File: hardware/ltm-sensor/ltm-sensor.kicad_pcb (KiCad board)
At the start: 2 copper layers, 89.7 x 53 mm, 22 parts, among them J1 KE PCB UTAMA, Q1 AO3400, U1 ITR20001 (S1), U2 ITR20001 (S2), U3 ITR20001 (S3), U4 ITR20001 (S4), U5 ITR20001 (S5)

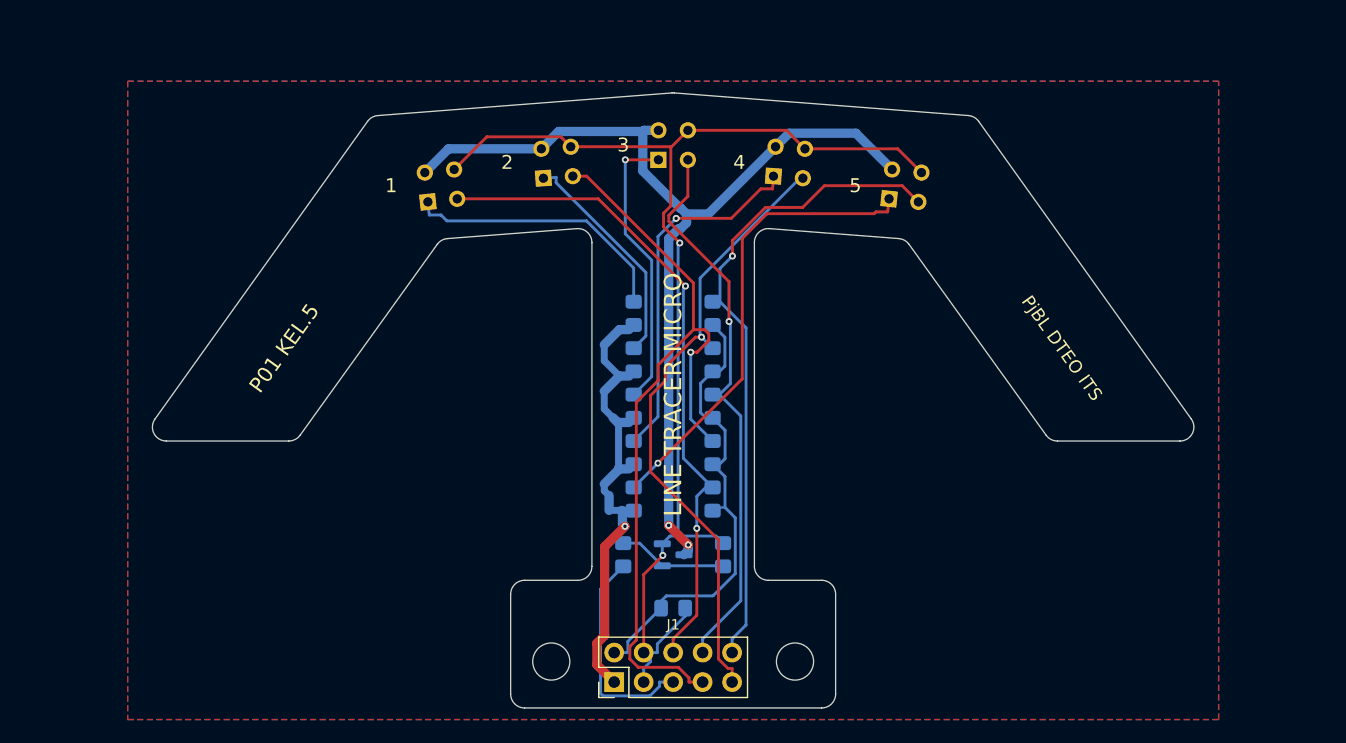
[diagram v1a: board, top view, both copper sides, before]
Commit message: Sensor 16 titik + mux + LED, kabel pita, aturan cetak 0,8 mm
- PCB sensor v2: batang lurus 110 x 51 mm, 16x ITR20001 (jarak 6,5 mm),
  modul mux CD74HC4067, MCP23017 + 16 LED indikator, box header IDC J1
- PCB utama: J5 jadi box header IDC 2x6 (kabel pita ke PCB sensor),
  pin ESP32 disusun ulang supaya jalur tidak saling silang
- Aturan tempat cetak: jalur >= 0,8 mm (daya 1,2), clearance 0,5,
  via 1,6/0,8; kedua PCB 0 jalur putus, DRC bersih
- Charter/RAB: 16 sensor, total Rp896.000
- Model 3D v12: PCB sensor batang di dudukan 3D print + kabel pita,
  STEP dan render diperbarui

Co-Authored-By: Claude Opus 5.5 <noreply@anthropic.com>
Claude-Session: https://claude.ai/code/session_016j7fGnGXJh3ke3RU3C9DKW
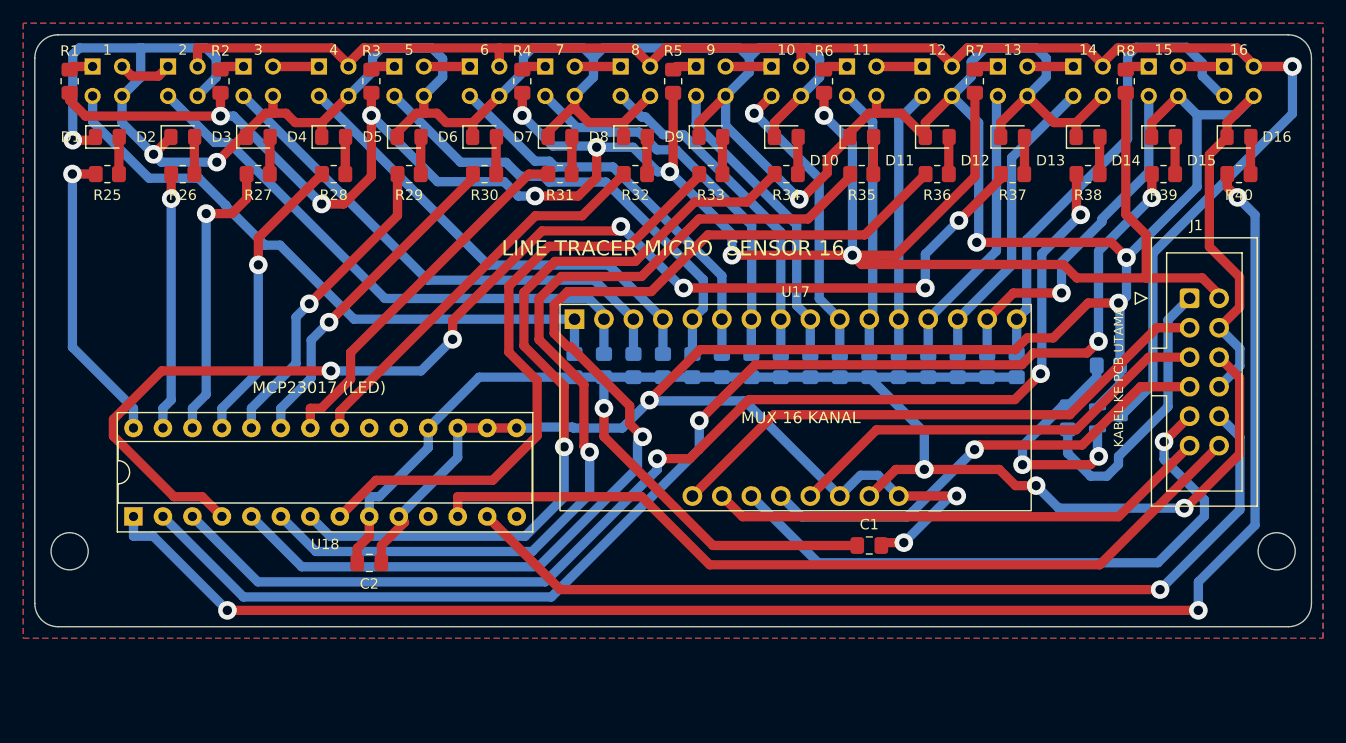
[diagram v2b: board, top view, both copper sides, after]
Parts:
- added C2: 100nF, Capacitor_SMD:C_0805_2012Metric_Pad1.18x1.45mm_HandSolder, F.Cu at (73.8, 58.5)
- added D1: LED, LED_SMD:LED_0805_2012Metric_Pad1.15x1.40mm_HandSolder, F.Cu at (51.2, 21.8)
- added D10: LED, LED_SMD:LED_0805_2012Metric_Pad1.15x1.40mm_HandSolder, F.Cu at (109.8, 21.8)
- added D11: LED, LED_SMD:LED_0805_2012Metric_Pad1.15x1.40mm_HandSolder, F.Cu at (116.2, 21.8)
- added D12: LED, LED_SMD:LED_0805_2012Metric_Pad1.15x1.40mm_HandSolder, F.Cu at (122.8, 21.8)
- added D13: LED, LED_SMD:LED_0805_2012Metric_Pad1.15x1.40mm_HandSolder, F.Cu at (129.2, 21.8)
- added D14: LED, LED_SMD:LED_0805_2012Metric_Pad1.15x1.40mm_HandSolder, F.Cu at (135.8, 21.8)
- added D15: LED, LED_SMD:LED_0805_2012Metric_Pad1.15x1.40mm_HandSolder, F.Cu at (142.2, 21.8)
- added D16: LED, LED_SMD:LED_0805_2012Metric_Pad1.15x1.40mm_HandSolder, F.Cu at (148.8, 21.8)
- added D2: LED, LED_SMD:LED_0805_2012Metric_Pad1.15x1.40mm_HandSolder, F.Cu at (57.8, 21.8)
- added D3: LED, LED_SMD:LED_0805_2012Metric_Pad1.15x1.40mm_HandSolder, F.Cu at (64.2, 21.8)
- added D4: LED, LED_SMD:LED_0805_2012Metric_Pad1.15x1.40mm_HandSolder, F.Cu at (70.8, 21.8)
- added D5: LED, LED_SMD:LED_0805_2012Metric_Pad1.15x1.40mm_HandSolder, F.Cu at (77.2, 21.8)
- added D6: LED, LED_SMD:LED_0805_2012Metric_Pad1.15x1.40mm_HandSolder, F.Cu at (83.8, 21.8)
- added D7: LED, LED_SMD:LED_0805_2012Metric_Pad1.15x1.40mm_HandSolder, F.Cu at (90.2, 21.8)
- added D8: LED, LED_SMD:LED_0805_2012Metric_Pad1.15x1.40mm_HandSolder, F.Cu at (96.8, 21.8)
- added D9: LED, LED_SMD:LED_0805_2012Metric_Pad1.15x1.40mm_HandSolder, F.Cu at (103.2, 21.8)
- added R13: 10k, Resistor_SMD:R_0805_2012Metric_Pad1.20x1.40mm_HandSolder, B.Cu at (101.7, 41.5)
- added R14: 10k, Resistor_SMD:R_0805_2012Metric_Pad1.20x1.40mm_HandSolder, B.Cu at (104.2, 41.5)
- added R15: 10k, Resistor_SMD:R_0805_2012Metric_Pad1.20x1.40mm_HandSolder, B.Cu at (106.7, 41.5)
- added R16: 10k, Resistor_SMD:R_0805_2012Metric_Pad1.20x1.40mm_HandSolder, B.Cu at (109.3, 41.5)
- added R17: 10k, Resistor_SMD:R_0805_2012Metric_Pad1.20x1.40mm_HandSolder, B.Cu at (111.8, 41.5)
- added R18: 10k, Resistor_SMD:R_0805_2012Metric_Pad1.20x1.40mm_HandSolder, B.Cu at (114.4, 41.5)
- added R19: 10k, Resistor_SMD:R_0805_2012Metric_Pad1.20x1.40mm_HandSolder, B.Cu at (116.9, 41.5)
- added R20: 10k, Resistor_SMD:R_0805_2012Metric_Pad1.20x1.40mm_HandSolder, B.Cu at (119.4, 41.5)
- added R21: 10k, Resistor_SMD:R_0805_2012Metric_Pad1.20x1.40mm_HandSolder, B.Cu at (122.0, 41.5)
- added R22: 10k, Resistor_SMD:R_0805_2012Metric_Pad1.20x1.40mm_HandSolder, B.Cu at (124.5, 41.5)
- added R23: 10k, Resistor_SMD:R_0805_2012Metric_Pad1.20x1.40mm_HandSolder, B.Cu at (127.1, 41.5)
- added R24: 10k, Resistor_SMD:R_0805_2012Metric_Pad1.20x1.40mm_HandSolder, B.Cu at (129.6, 41.5)
- added R25: 330, Resistor_SMD:R_0805_2012Metric_Pad1.20x1.40mm_HandSolder, F.Cu at (51.2, 25.0)
- added R26: 330, Resistor_SMD:R_0805_2012Metric_Pad1.20x1.40mm_HandSolder, F.Cu at (57.8, 25.0)
- added R27: 330, Resistor_SMD:R_0805_2012Metric_Pad1.20x1.40mm_HandSolder, F.Cu at (64.2, 25.0)
- added R28: 330, Resistor_SMD:R_0805_2012Metric_Pad1.20x1.40mm_HandSolder, F.Cu at (70.8, 25.0)
- added R29: 330, Resistor_SMD:R_0805_2012Metric_Pad1.20x1.40mm_HandSolder, F.Cu at (77.2, 25.0)
- added R30: 330, Resistor_SMD:R_0805_2012Metric_Pad1.20x1.40mm_HandSolder, F.Cu at (83.8, 25.0)
- added R31: 330, Resistor_SMD:R_0805_2012Metric_Pad1.20x1.40mm_HandSolder, F.Cu at (90.2, 25.0)
- added R32: 330, Resistor_SMD:R_0805_2012Metric_Pad1.20x1.40mm_HandSolder, F.Cu at (96.8, 25.0)
- added R33: 330, Resistor_SMD:R_0805_2012Metric_Pad1.20x1.40mm_HandSolder, F.Cu at (103.2, 25.0)
- added R34: 330, Resistor_SMD:R_0805_2012Metric_Pad1.20x1.40mm_HandSolder, F.Cu at (109.8, 25.0)
- added R35: 330, Resistor_SMD:R_0805_2012Metric_Pad1.20x1.40mm_HandSolder, F.Cu at (116.2, 25.0)
- added R36: 330, Resistor_SMD:R_0805_2012Metric_Pad1.20x1.40mm_HandSolder, F.Cu at (122.8, 25.0)
- added R37: 330, Resistor_SMD:R_0805_2012Metric_Pad1.20x1.40mm_HandSolder, F.Cu at (129.2, 25.0)
- added R38: 330, Resistor_SMD:R_0805_2012Metric_Pad1.20x1.40mm_HandSolder, F.Cu at (135.8, 25.0)
- added R39: 330, Resistor_SMD:R_0805_2012Metric_Pad1.20x1.40mm_HandSolder, F.Cu at (142.2, 25.0)
- added R40: 330, Resistor_SMD:R_0805_2012Metric_Pad1.20x1.40mm_HandSolder, F.Cu at (148.8, 25.0)
- added R41: 100, Resistor_SMD:R_0805_2012Metric_Pad1.20x1.40mm_HandSolder, B.Cu at (134.0, 46.0)
- added R42: 10k, Resistor_SMD:R_0805_2012Metric_Pad1.20x1.40mm_HandSolder, B.Cu at (137.5, 41.5)
- added U10: ITR20001 (S10), ltm:ITR20001, B.Cu at (109.8, 17.0)
- added U11: ITR20001 (S11), ltm:ITR20001, B.Cu at (116.2, 17.0)
- added U12: ITR20001 (S12), ltm:ITR20001, B.Cu at (122.8, 17.0)
- added U13: ITR20001 (S13), ltm:ITR20001, B.Cu at (129.2, 17.0)
- added U14: ITR20001 (S14), ltm:ITR20001, B.Cu at (135.8, 17.0)
- added U15: ITR20001 (S15), ltm:ITR20001, B.Cu at (142.2, 17.0)
- added U16: ITR20001 (S16), ltm:ITR20001, B.Cu at (148.8, 17.0)
- added U17: Modul CD74HC4067, ltm:CD74HC4067_Module, F.Cu at (91.5, 37.5)
- added U18: MCP23017, Package_DIP:DIP-28_W7.62mm_Socket, F.Cu at (53.5, 54.5)
- added U6: ITR20001 (S6), ltm:ITR20001, B.Cu at (83.8, 17.0)
- added U7: ITR20001 (S7), ltm:ITR20001, B.Cu at (90.2, 17.0)
- added U8: ITR20001 (S8), ltm:ITR20001, B.Cu at (96.8, 17.0)
- added U9: ITR20001 (S9), ltm:ITR20001, B.Cu at (103.2, 17.0)
- C1: moved to F.Cu
- J1: value KE PCB UTAMA -> KABEL PITA 12 PIN; footprint Connector_PinHeader_2.54mm:PinHeader_2x05_P2.54mm_Vertical -> Connector_IDC:IDC-Header_2x06_P2.54mm_Vertical
- R1, R2, R3, R4, R5: value 180 -> 120; moved to F.Cu
- R11: value 100 -> 10k
- R6, R7, R8: value 10k -> 120; moved to F.Cu
- moved J1 59.6 mm to (144.5, 35.7), turned to 0 degrees
- moved R1 52.6 mm to (48.0, 17.0)
- moved R8 45.3 mm to (139.0, 17.0)
- moved U5 43.7 mm to (77.2, 17.0), turned to -90 degrees
- moved R2 42.9 mm to (61.0, 17.0)
- moved H1 42.6 mm to (48.0, 57.5)
- moved H2 42.6 mm to (152.0, 57.5)
- moved U4 39.9 mm to (70.8, 17.0), turned to -90 degrees
- moved Q1 39.3 mm to (137.5, 46.0)
- moved R7 39.2 mm to (126.0, 17.0)
- moved R6 37.3 mm to (113.0, 17.0)
- moved U3 36.2 mm to (64.2, 17.0), turned to -90 degrees
- moved R5 36.2 mm to (100.0, 17.0)
- moved R3 36.0 mm to (74.0, 17.0)
- moved R4 33.4 mm to (87.0, 17.0)
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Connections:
- net /LED_A1 renamed /IR_A1
- J1 pad 1: +5V -> /IR_EN
- J1 pad 10: /S5 -> /SDA
- J1 pad 2: +3V3 -> +5V
- J1 pad 3: GND -> /SIG
- J1 pad 5: /IR_EN -> /MUX_S0
- J1 pad 6: /S1 -> +3V3
- J1 pad 7: /S2 -> /MUX_S1
- J1 pad 8: /S3 -> GND
- J1 pad 9: /S4 -> /MUX_S2
- R10 pad 2: /S5 -> /S2
- R11 pad 1: /IR_EN -> +3V3
- R11 pad 2: /IR_G -> /S3
- R12 pad 1: /IR_G -> +3V3
- R12 pad 2: GND -> /S4
- R2 pad 2: /LED_A2 -> /IR_A2
- R3 pad 2: /LED_A3 -> /IR_A3
- R4 pad 2: /LED_A4 -> /IR_A4
- R5 pad 2: /LED_A5 -> /IR_A5
- R6 pad 1: +3V3 -> +5V
- R6 pad 2: /S1 -> /IR_A6
- R7 pad 1: +3V3 -> +5V
- R7 pad 2: /S2 -> /IR_A7
- R8 pad 1: +3V3 -> +5V
- R8 pad 2: /S3 -> /IR_A8
- R9 pad 2: /S4 -> /S1
- U1 pad 2: /LED_K -> /IR_M1
- U2 pad 1: /LED_A2 -> /IR_M1
- U3 pad 1: /LED_A3 -> /IR_A2
- U3 pad 2: /LED_K -> /IR_M2
- U4 pad 1: /LED_A4 -> /IR_M2
- U5 pad 1: /LED_A5 -> /IR_A3
- U5 pad 2: /LED_K -> /IR_M3
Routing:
- net GND: track 103.0 -> 434.0 mm, vias 2 -> 10
- net +5V: track 42.8 -> 195.0 mm, vias 1 -> 10
- net /LD16: track 0.00 -> 136.7 mm, vias 0 -> 3
- net +3V3: track 41.1 -> 153.1 mm, vias 0 -> 4
- net /LD15: track 0.00 -> 110.4 mm, vias 0 -> 3
- net /LD13: track 0.00 -> 106.2 mm, vias 0 -> 6
- net /LD14: track 0.00 -> 102.2 mm, vias 0 -> 3
- net /LD12: track 0.00 -> 92.8 mm, vias 0 -> 1
- net /LD11: track 0.00 -> 79.9 mm, vias 0 -> 1
- net /SDA: track 0.00 -> 79.1 mm, vias 0 -> 1
- net /SCL: track 0.00 -> 74.0 mm
- net /LD10: track 0.00 -> 68.9 mm, vias 0 -> 1
- net /LED_K: track 83.2 -> 141.9 mm, vias 2 -> 1
- net /LD9: track 0.00 -> 54.3 mm
- net /MUX_S2: track 0.00 -> 54.1 mm, vias 0 -> 1
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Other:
- board size 89.7 x 53 mm -> 110 x 51 mm
- board text added: "10"
- board text added: "11"
- board text added: "12"
- board text added: "13"
- board text added: "14"
- board text added: "15"
- board text added: "16"
- board text added: "6"
- board text added: "7"
- board text added: "8"
- board text added: "9"
- board text added: "KABEL KE PCB UTAMA"
- board text added: "LINE TRACER MICRO SENSOR 16"
- board text added: "MCP23017 (LED)"
- board text added: "MUX 16 KANAL"
- board text removed: "LINE TRACER MICRO"
- board text removed: "P01 KEL.5"
- board text removed: "PjBL DTEO ITS"
